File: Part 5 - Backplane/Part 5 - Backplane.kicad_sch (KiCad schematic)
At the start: 37 parts, among them J1 BUS 1, J10 EXTENDED BUS, J11 5V DC, J2 BUS 2, J3 BUS 3, J4 BUS 4, J5 BUS 5, J6 BUS 6, J7 BUS 7, J8 BUS 8, J9 BASIC BUS, U1 LD1117AV33

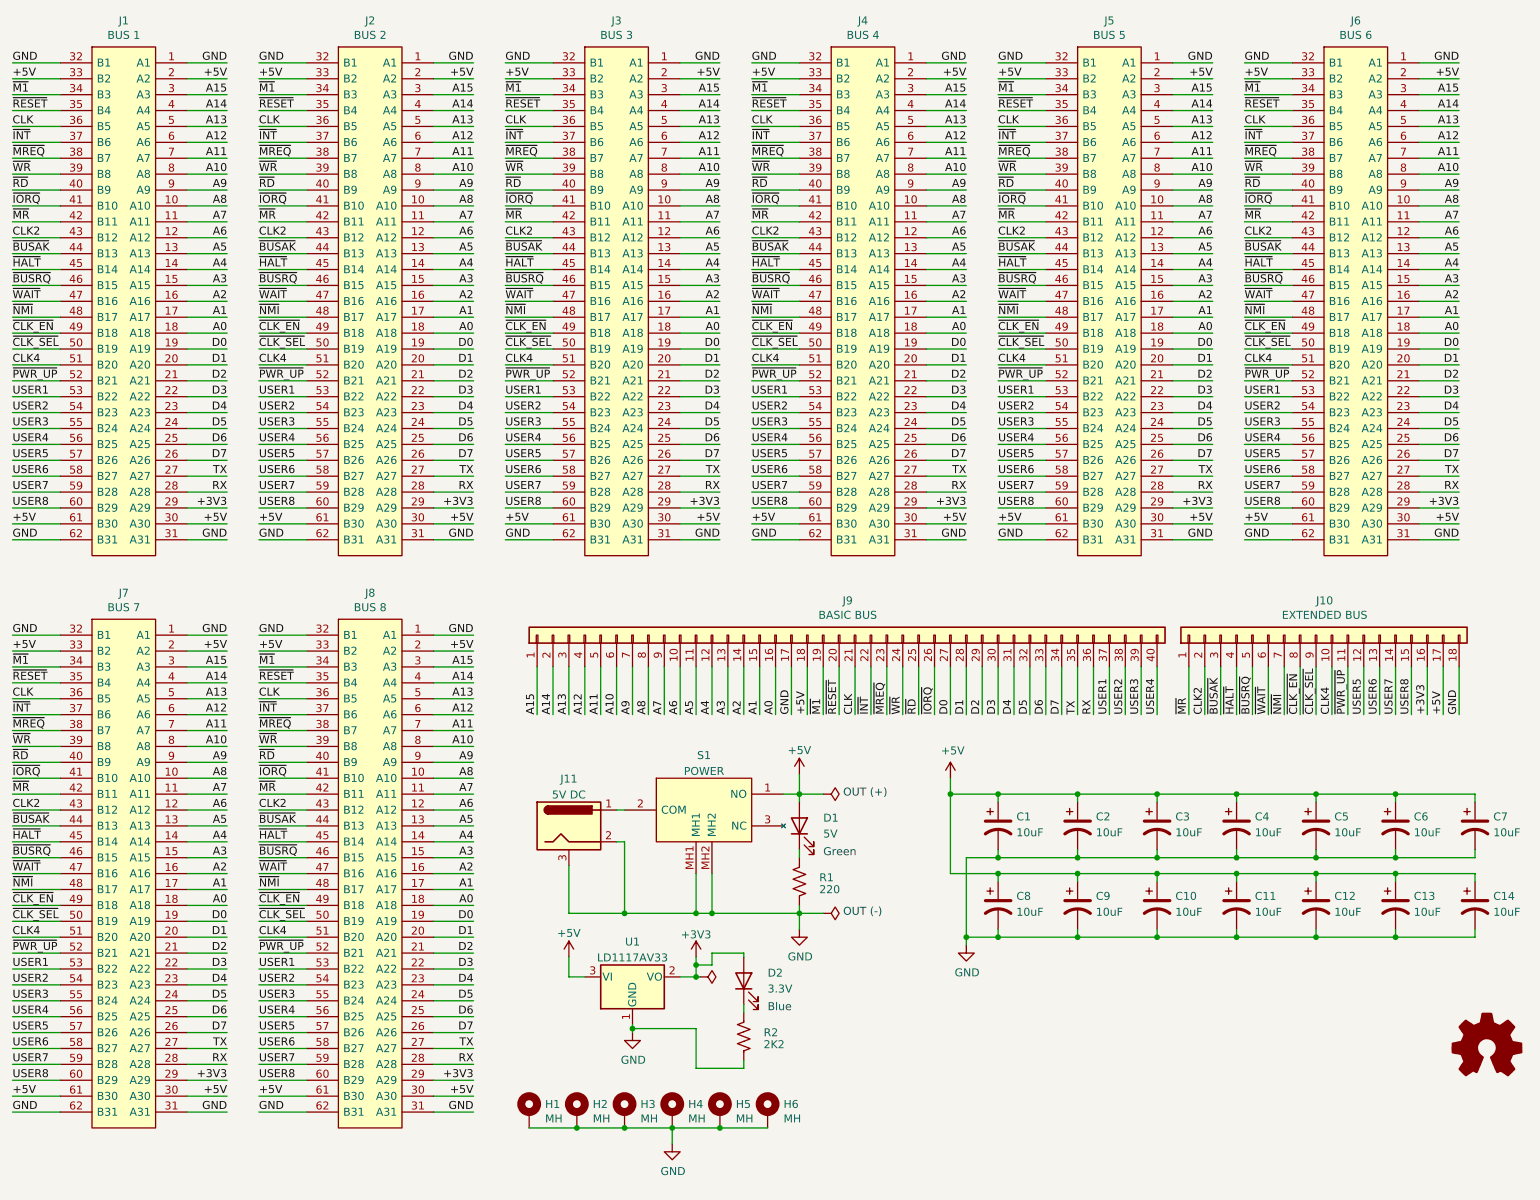
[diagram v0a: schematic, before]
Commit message: Changed the clock for even cleaner clock switching
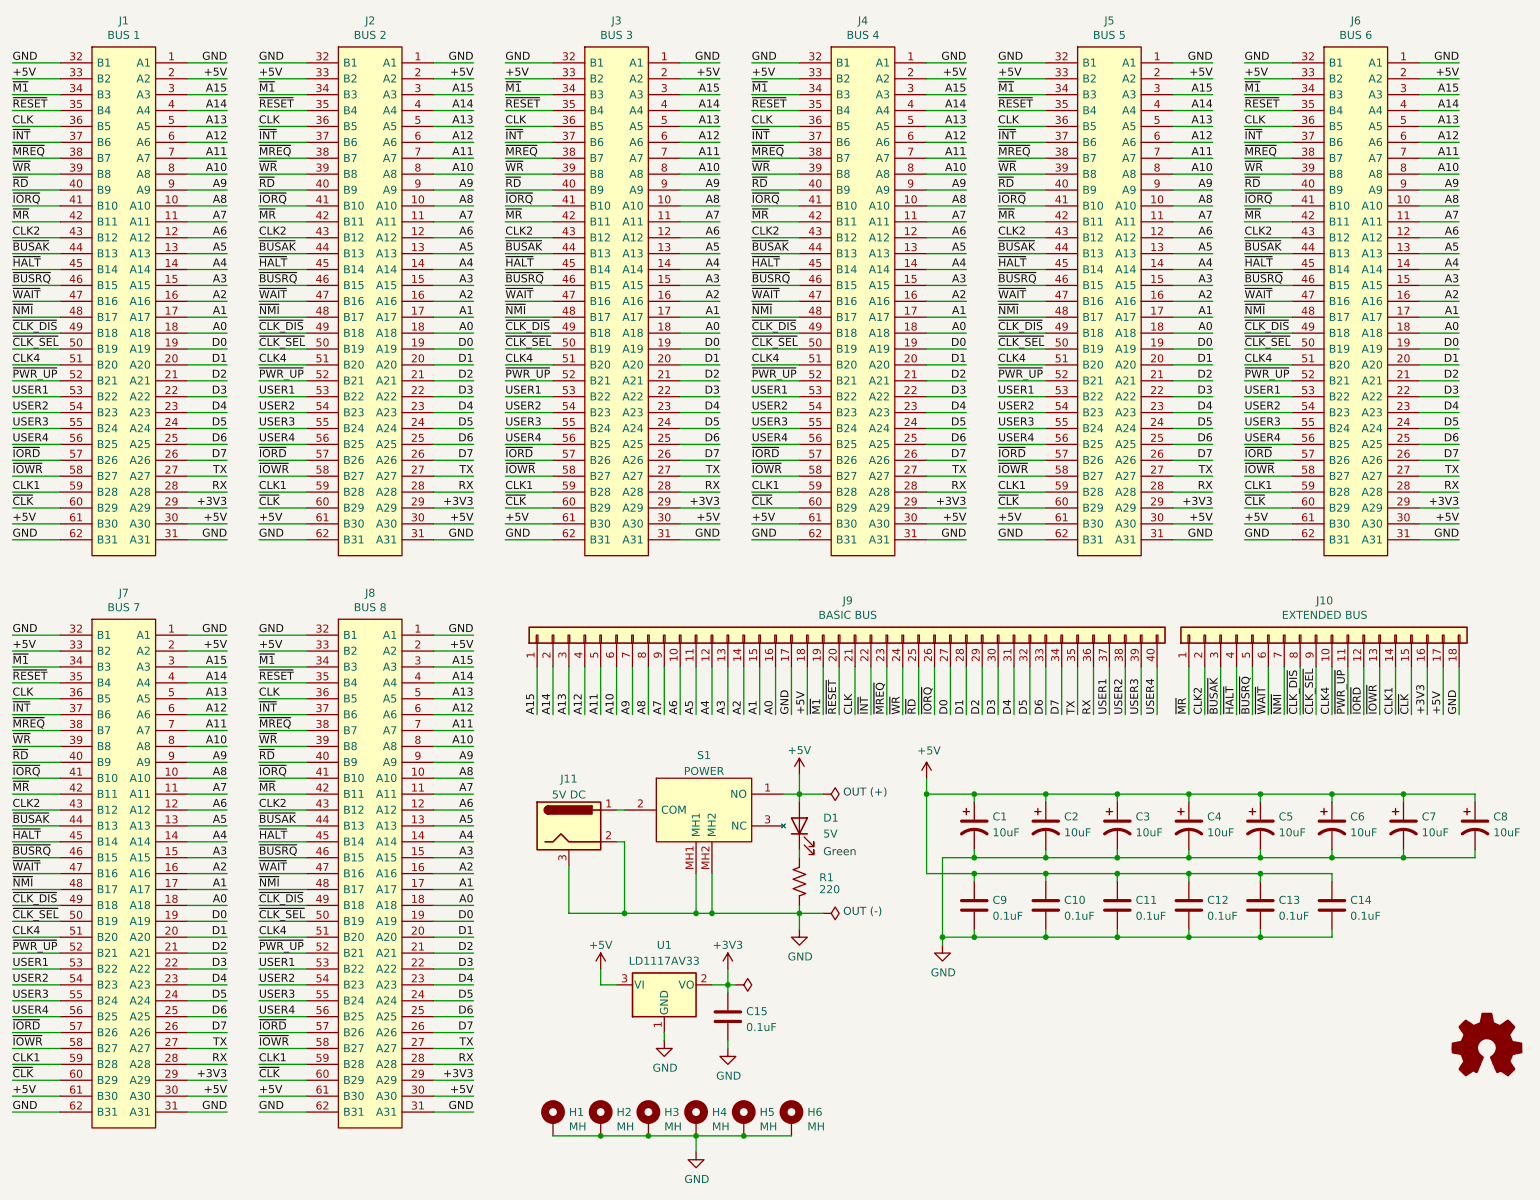
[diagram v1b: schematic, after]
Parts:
- removed C11, C13, C2, C4, C6, C9: 10uF, Capacitor_THT:CP_Radial_D6.3mm_P2.50mm, symbol Device:C_Polarized_US
- removed D2: 3.3V, LED_THT:LED_D3.0mm, symbol Device:LED
- removed R2: 2K2, Resistor_THT:R_Axial_DIN0207_L6.3mm_D2.5mm_P10.16mm_Horizontal, symbol Device:R_US
- added C10, C11, C12, C13, C14, C15, C9: 0.1uF, Capacitor_THT:C_Disc_D3.0mm_W2.0mm_P2.50mm, symbol Device:C
- renumbered C3 to C2, C5 to C3, C7 to C4, C8 to C5, C10 to C6, C12 to C7, C14 to C8
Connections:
- net +3V3: now also C15.1
- net +5V: now also C10.1, C11.1, C12.1, C13.1, C14.1, C9.1
- net GND: now also C10.2, C11.2, C12.2, C13.2, C14.2, C15.2, C9.2
- net USER5 renamed ~{IORD}
- net USER6 renamed ~{IOWR}
- net USER7 renamed CLK1
- net USER8 renamed ~{CLK}
- net ~{CLK_EN} renamed ~{CLK_DIS}
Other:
- note removed: "Blue"
- moved on the sheet: C1, C2, C3, C4, C5, C6, C7, C8, H1, H2, H3, H4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

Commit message: Added Keyboard, and minor fixes
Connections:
- net ~{IORD} renamed USER5
- net ~{IOWR} renamed USER6
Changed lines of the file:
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@@
     (effects (font (size 1.27 1.27)) (justify left bottom))
   )
-  (label "~{IOWR}" (at 140.97 88.9 0)
+  (label "USER6" (at 140.97 88.9 0)
     (effects (font (size 1.27 1.27)) (justify left bottom))
   )
@@
     (effects (font (size 1.27 1.27)) (justify right bottom))
   )
-  (label "~{IOWR}" (at 22.86 180.34 0)
+  (label "USER6" (at 22.86 180.34 0)
     (effects (font (size 1.27 1.27)) (justify left bottom))
   )
@@
     (effects (font (size 1.27 1.27)) (justify left bottom))
   )
-  (label "~{IORD}" (at 62.23 177.8 0)
+  (label "USER5" (at 62.23 177.8 0)
     (effects (font (size 1.27 1.27)) (justify left bottom))
   )
@@
     (effects (font (size 1.27 1.27)) (justify left bottom))
   )
-  (label "~{IORD}" (at 22.86 177.8 0)
+  (label "USER5" (at 22.86 177.8 0)
     (effects (font (size 1.27 1.27)) (justify left bottom))
   )
@@
     (effects (font (size 1.27 1.27)) (justify right bottom))
   )
-  (label "~{IOWR}" (at 180.34 88.9 0)
+  (label "USER6" (at 180.34 88.9 0)
     (effects (font (size 1.27 1.27)) (justify left bottom))
   )
@@
     (effects (font (size 1.27 1.27)) (justify right bottom))
   )
-  (label "~{IORD}" (at 140.97 86.36 0)
+  (label "USER5" (at 140.97 86.36 0)
     (effects (font (size 1.27 1.27)) (justify left bottom))
   )
@@
     (effects (font (size 1.27 1.27)) (justify right bottom))
   )
-  (label "~{IOWR}" (at 219.71 88.9 0)
+  (label "USER6" (at 219.71 88.9 0)
     (effects (font (size 1.27 1.27)) (justify left bottom))
   )
@@
     (effects (font (size 1.27 1.27)) (justify right bottom))
   )
-  (label "~{IORD}" (at 62.23 86.36 0)
+  (label "USER5" (at 62.23 86.36 0)
     (effects (font (size 1.27 1.27)) (justify left bottom))
   )
@@
     (effects (font (size 1.27 1.27)) (justify left bottom))
   )
-  (label "~{IORD}" (at 180.34 86.36 0)
+  (label "USER5" (at 180.34 86.36 0)
     (effects (font (size 1.27 1.27)) (justify left bottom))
   )
@@
     (effects (font (size 1.27 1.27)) (justify right bottom))
   )
-  (label "~{IOWR}" (at 62.23 88.9 0)
+  (label "USER6" (at 62.23 88.9 0)
     (effects (font (size 1.27 1.27)) (justify left bottom))
   )
@@
     (effects (font (size 1.27 1.27)) (justify right bottom))
   )
-  (label "~{IORD}" (at 101.6 86.36 0)
+  (label "USER5" (at 101.6 86.36 0)
     (effects (font (size 1.27 1.27)) (justify left bottom))
   )
@@
     (effects (font (size 1.27 1.27)) (justify left bottom))
   )
-  (label "~{IOWR}" (at 101.6 88.9 0)
+  (label "USER6" (at 101.6 88.9 0)
     (effects (font (size 1.27 1.27)) (justify left bottom))
   )
@@
     (effects (font (size 1.27 1.27)) (justify left bottom))
   )
-  (label "~{IORD}" (at 238.76 127 90)
+  (label "USER5" (at 238.76 127 90)
     (effects (font (size 1.27 1.27)) (justify left bottom))
   )
@@
     (effects (font (size 1.27 1.27)) (justify left bottom))
   )
-  (label "~{IOWR}" (at 22.86 88.9 0)
+  (label "USER6" (at 22.86 88.9 0)
     (effects (font (size 1.27 1.27)) (justify left bottom))
   )
@@
     (effects (font (size 1.27 1.27)) (justify left bottom))
   )
-  (label "~{IOWR}" (at 241.3 127 90)
+  (label "USER6" (at 241.3 127 90)
     (effects (font (size 1.27 1.27)) (justify left bottom))
   )
@@
     (effects (font (size 1.27 1.27)) (justify left bottom))
   )
-  (label "~{IORD}" (at 219.71 86.36 0)
+  (label "USER5" (at 219.71 86.36 0)
     (effects (font (size 1.27 1.27)) (justify left bottom))
   )
@@
     (effects (font (size 1.27 1.27)) (justify right bottom))
   )
-  (label "~{IORD}" (at 22.86 86.36 0)
+  (label "USER5" (at 22.86 86.36 0)
     (effects (font (size 1.27 1.27)) (justify left bottom))
   )
@@
     (effects (font (size 1.27 1.27)) (justify left bottom))
   )
-  (label "~{IOWR}" (at 62.23 180.34 0)
-    (effects (font (size 1.27 1.27)) (justify left bottom))
-  )
+  (label "USER6" (at 62.23 180.34 0)
+    (effects (font (size 1.27 1.27)) (justify left bottom))
+  )

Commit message: Long time backup
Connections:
- net ~{MR} is gone; now on net ~{CLK}: J1.42 (B11), J10.1 (Pin_1), J2.42 (B11), J3.42 (B11), J4.42 (B11), J5.42 (B11), J6.42 (B11), J7.42 (B11), J8.42 (B11)
- net USER1: now also J1.49 (B18), J2.49 (B18), J3.49 (B18), J4.49 (B18), J5.49 (B18), J6.49 (B18), J7.49 (B18), J8.49 (B18); no longer J1.53 (B22), J2.53 (B22), J3.53 (B22), J4.53 (B22), J5.53 (B22), J6.53 (B22), J7.53 (B22), J8.53 (B22)
- net USER2: now also J1.50 (B19), J2.50 (B19), J3.50 (B19), J4.50 (B19), J5.50 (B19), J6.50 (B19), J7.50 (B19), J8.50 (B19); no longer J1.54 (B23), J2.54 (B23), J3.54 (B23), J4.54 (B23), J5.54 (B23), J6.54 (B23), J7.54 (B23), J8.54 (B23)
- net USER3: now also J1.51 (B20), J2.51 (B20), J3.51 (B20), J4.51 (B20), J5.51 (B20), J6.51 (B20), J7.51 (B20), J8.51 (B20); no longer J1.55 (B24), J2.55 (B24), J3.55 (B24), J4.55 (B24), J5.55 (B24), J6.55 (B24), J7.55 (B24), J8.55 (B24)
- net USER4: now also J1.52 (B21), J2.52 (B21), J3.52 (B21), J4.52 (B21), J5.52 (B21), J6.52 (B21), J7.52 (B21), J8.52 (B21); no longer J1.56 (B25), J2.56 (B25), J3.56 (B25), J4.56 (B25), J5.56 (B25), J6.56 (B25), J7.56 (B25), J8.56 (B25)
- net ~{CLK}: no longer J1.60 (B29), J10.15 (Pin_15), J2.60 (B29), J3.60 (B29), J4.60 (B29), J5.60 (B29), J6.60 (B29), J7.60 (B29), J8.60 (B29)
- net CLK1 renamed ~{IRQ8}
- removed net CLK4: J1.51 (B20), J10.10 (Pin_10), J2.51 (B20), J3.51 (B20), J4.51 (B20), J5.51 (B20), J6.51 (B20), J7.51 (B20), J8.51 (B20)
- net USER5 renamed ~{IRQ6}
- net USER6 renamed ~{IRQ7}
- removed net ~{CLK_DIS}: J1.49 (B18), J10.8 (Pin_8), J2.49 (B18), J3.49 (B18), J4.49 (B18), J5.49 (B18), J6.49 (B18), J7.49 (B18), J8.49 (B18)
- removed net ~{CLK_SEL}: J1.50 (B19), J10.9 (Pin_9), J2.50 (B19), J3.50 (B19), J4.50 (B19), J5.50 (B19), J6.50 (B19), J7.50 (B19), J8.50 (B19)
- removed net ~{PWR_UP}: J1.52 (B21), J10.11 (Pin_11), J2.52 (B21), J3.52 (B21), J4.52 (B21), J5.52 (B21), J6.52 (B21), J7.52 (B21), J8.52 (B21)
- new net ~{IRQ1}: J1.53 (B22), J10.8 (Pin_8), J2.53 (B22), J3.53 (B22), J4.53 (B22), J5.53 (B22), J6.53 (B22), J7.53 (B22), J8.53 (B22)
- new net ~{IRQ2}: J1.54 (B23), J10.9 (Pin_9), J2.54 (B23), J3.54 (B23), J4.54 (B23), J5.54 (B23), J6.54 (B23), J7.54 (B23), J8.54 (B23)
- new net ~{IRQ3}: J1.55 (B24), J10.10 (Pin_10), J2.55 (B24), J3.55 (B24), J4.55 (B24), J5.55 (B24), J6.55 (B24), J7.55 (B24), J8.55 (B24)
- new net ~{IRQ5}: J1.56 (B25), J10.11 (Pin_11), J2.56 (B25), J3.56 (B25), J4.56 (B25), J5.56 (B25), J6.56 (B25), J7.56 (B25), J8.56 (B25)
- new net ~{IRQ9}: J1.60 (B29), J10.15 (Pin_15), J2.60 (B29), J3.60 (B29), J4.60 (B29), J5.60 (B29), J6.60 (B29), J7.60 (B29), J8.60 (B29)
